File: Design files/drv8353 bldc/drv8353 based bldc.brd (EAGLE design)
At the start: 127 x 127 mm, 115 parts, among them IC1 DRV8353RSRGZT, J3 2X6 FEMALE, J4 B06B-HCMKK

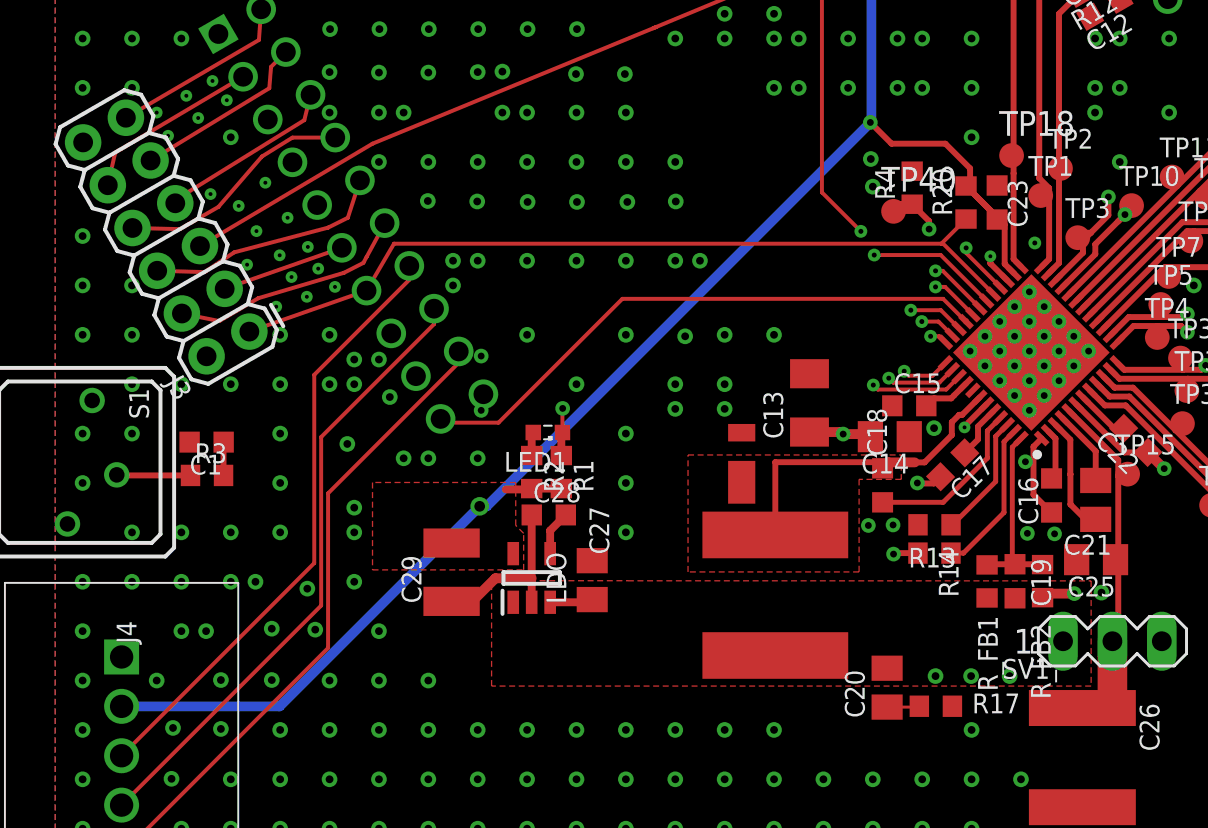
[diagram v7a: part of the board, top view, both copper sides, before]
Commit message: adds zener and bypas header for LDO
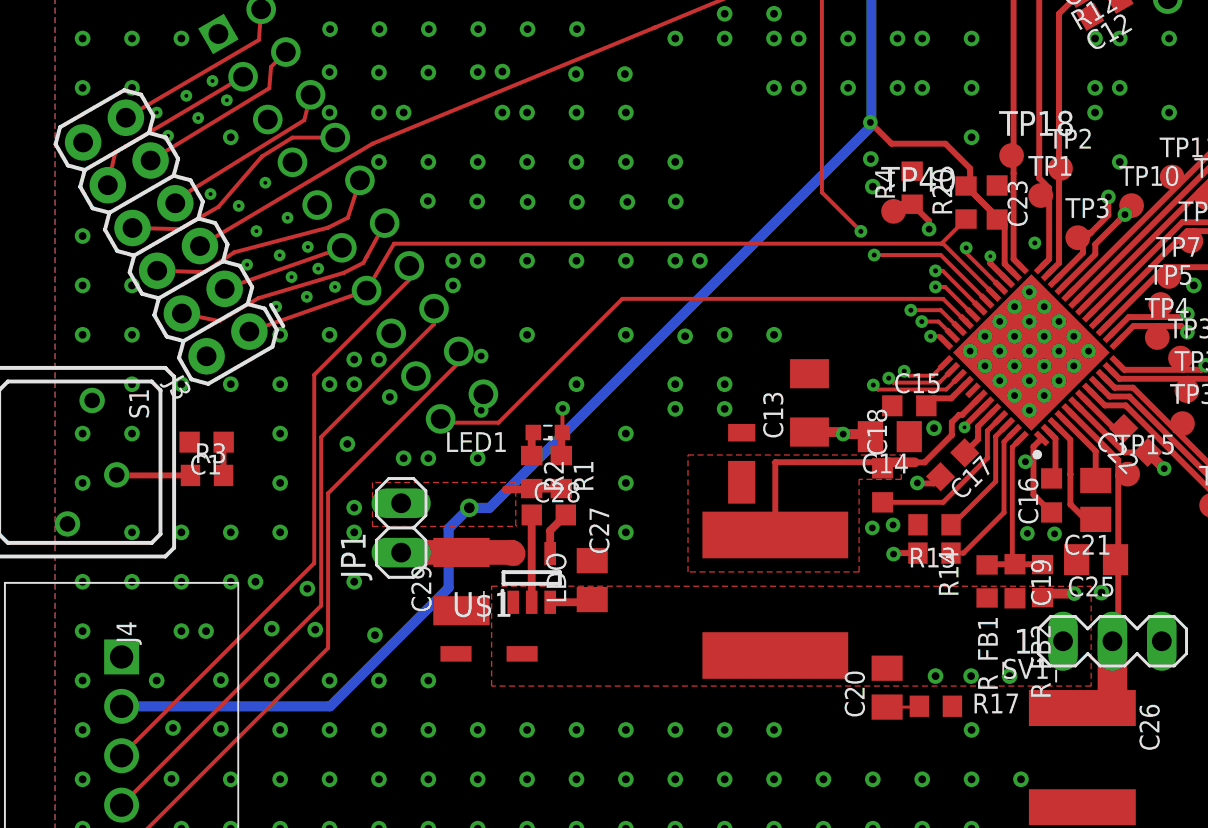
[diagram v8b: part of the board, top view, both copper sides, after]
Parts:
- added JP1: (no value), pinhead:1X02
- added U$1: ZENER, REV BLDC:SOD123
- moved C29 0.70 mm to (24.6, 69.9)
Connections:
- removed net N$5: C28.1, C29.1, LDO.2
- new net N$2: C29.2, JP1.1, LDO.5
- net 3V3: now also JP1.2; no longer C29.2, LDO.5
- net GND: now also C28.1, C29.1, LDO.2, U$1.1
- net VBUCK: now also U$1.2
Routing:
- net N$5: track 9.11 -> 0.00 mm
- net N$2: track 0.00 -> 5.79 mm
- net GND: track 7.95 -> 12.5 mm
- net 3V3: track 101.9 -> 103.8 mm
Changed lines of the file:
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@@
 <attribute name="SPICEPREFIX" value="C" x="72.2346" y="-49.9038" size="1.778" layer="27" display="off"/>
 </element>
-<element name="C29" library="rcl" library_urn="urn:adsk.eagle:library:334" package="C1210K" package3d_urn="urn:adsk.eagle:package:23683/2" value="4.7 uF" x="24.0556" y="70.3408" smashed="yes" rot="R90">
-<attribute name="NAME" x="22.5056" y="68.7408" size="1.016" layer="25" rot="R90"/>
-<attribute name="POPULARITY" value="0" x="124.3856" y="112.2508" size="1.778" layer="27" rot="R90" display="off"/>
-<attribute name="SPICEPREFIX" value="C" x="124.3856" y="112.2508" size="1.778" layer="27" rot="R90" display="off"/>
+<element name="C29" library="rcl" library_urn="urn:adsk.eagle:library:334" package="C1210K" package3d_urn="urn:adsk.eagle:package:23683/2" value="4.7 uF" x="24.5636" y="69.8582" smashed="yes" rot="R90">
+<attribute name="NAME" x="23.0136" y="68.2582" size="1.016" layer="25" rot="R90"/>
+<attribute name="POPULARITY" value="0" x="124.8936" y="111.7682" size="1.778" layer="27" rot="R90" display="off"/>
+<attribute name="SPICEPREFIX" value="C" x="124.8936" y="111.7682" size="1.778" layer="27" rot="R90" display="off"/>
 </element>
 <element name="C30" library="rcl" library_urn="urn:adsk.eagle:library:334" package="C1206" package3d_urn="urn:adsk.eagle:package:23618/2" value="1uF" x="79.2208" y="97.1468" smashed="yes" rot="R180">
@@
 </element>
 <element name="LED1" library="eagle-ltspice" library_urn="urn:adsk.eagle:library:217" package="LED_SML0603" package3d_urn="urn:adsk.eagle:package:13315/1" value="" x="29.0078" y="77.5258" smashed="yes" rot="R180">
-<attribute name="NAME" x="30.0078" y="76.5258" size="1.016" layer="25" rot="R180"/>
+<attribute name="NAME" x="26.9598" y="77.5418" size="1.016" layer="25" rot="R180"/>
 <attribute name="SPICEMODEL" value="NONE" x="-4.0122" y="215.9558" size="1.778" layer="27" rot="R180" display="off"/>
 <attribute name="SPICEPREFIX" value="D" x="-4.0122" y="215.9558" size="1.778" layer="27" rot="R180" display="off"/>
@@
 <attribute name="VALUE" x="91.821" y="111.379" size="1.27" layer="27" rot="R180"/>
 </element>
+<element name="U$1" library="REV BLDC" package="SOD123" package3d_urn="urn:adsk.eagle:package:26308/2" value="ZENER" x="25.9842" y="66.1416" smashed="yes">
+<attribute name="NAME" x="24.0792" y="68.0466" size="1.27" layer="25"/>
+<attribute name="VALUE" x="24.0792" y="62.9666" size="1.27" layer="27"/>
+</element>
+<element name="JP1" library="pinhead" library_urn="urn:adsk.eagle:library:325" package="1X02" package3d_urn="urn:adsk.eagle:package:22435/2" value="" x="21.463" y="72.6186" smashed="yes" rot="R90">
+<attribute name="NAME" x="19.6342" y="70.0024" size="1.27" layer="25" ratio="10" rot="R90"/>
+<attribute name="POPULARITY" value="98" x="21.463" y="72.6186" size="1.778" layer="27" rot="R90" display="off"/>
+<attribute name="VALUE" x="24.638" y="70.0786" size="1.27" layer="27" rot="R90"/>
+</element>
 </elements>
 <signals>
@@
 <vertex x="57.3278" y="12.1158"/>
 </polygon>
-<via x="45.4914" y="72.7456" extent="1-16" drill="0.35"/>
+<via x="45.6946" y="72.6186" extent="1-16" drill="0.35"/>
 <polygon width="0.3048" layer="1" thermals="no">
 <vertex x="3.7338" y="2.9718"/>
@@
 <via x="7.62" y="85.09" extent="1-16" drill="0.4"/>
 <via x="5.08" y="87.63" extent="1-16" drill="0.4"/>
-<via x="20.32" y="67.31" extent="1-16" drill="0.4"/>
+<via x="20.1168" y="67.1068" extent="1-16" drill="0.4"/>
 <via x="33.02" y="72.39" extent="1-16" drill="0.4"/>
 <via x="33.02" y="74.93" extent="1-16" drill="0.4"/>
@@
 <wire x1="54.6602" y1="69.2404" x2="56.0832" y2="69.2404" width="0.508" layer="1"/>
 <via x="48.8696" y="77.7494" extent="1-16" drill="0.4"/>
+<contactref element="U$1" pad="1"/>
+<contactref element="LDO" pad="2"/>
+<contactref element="C28" pad="1"/>
+<contactref element="C29" pad="1"/>
+<wire x1="28.1758" y1="68.7944" x2="28.1758" y2="73.2824" width="0.4064" layer="1"/>
+<wire x1="28.1758" y1="73.2824" x2="28.1796" y2="73.2862" width="0.4064" layer="1"/>
+<wire x1="24.5636" y1="68.3582" x2="24.6398" y2="68.3582" width="0.508" layer="1"/>
 </signal>
 <signal name="SNA">
@@
 <polygon width="0.1524" layer="1" isolate="0.254" thermals="no">
 <vertex x="26.1138" y="64.486"/>
-<vertex x="26.1138" y="69.9034"/>
-<vertex x="33.1216" y="69.9034"/>
-<vertex x="33.1216" y="69.900275"/>
-<vertex x="56.9484" y="69.894834375"/>
+<vertex x="26.1138" y="69.620875"/>
+<vertex x="56.9484" y="69.615428125"/>
+<vertex x="56.9484" y="69.615428125"/>
 <vertex x="56.9484" y="64.486"/>
 </polygon>
 <wire x1="31.2898" y1="68.9334" x2="31.1508" y2="68.7944" width="0.4064" layer="1"/>
 <wire x1="31.1508" y1="68.7944" x2="29.1258" y2="68.7944" width="0.4064" layer="1"/>
+<contactref element="U$1" pad="2"/>
 </signal>
 <signal name="FB">
@@
 <contactref element="R2" pad="2"/>
 <contactref element="U$2" pad="1"/>
-<contactref element="LDO" pad="5"/>
-<contactref element="C29" pad="2"/>
 <contactref element="IC1" pad="26"/>
 <polygon width="0.127" layer="1" thermals="no">
-<vertex x="19.9898" y="70.4596"/>
-<vertex x="27.7622" y="70.4596"/>
-<vertex x="27.7622" y="72.3392"/>
+<vertex x="19.9898" y="72.6948"/>
+<vertex x="27.4066" y="72.6948"/>
 <vertex x="27.3558" y="72.7456"/>
 <vertex x="27.3558" y="74.9554"/>
@@
 </polygon>
 <contactref element="J4" pad="2"/>
-<wire x1="7.0848" y1="63.4418" x2="15.214" y2="63.4418" width="0.508" layer="16"/>
-<wire x1="25.5016" y1="73.7294" x2="15.214" y2="63.4418" width="0.508" layer="16"/>
-<via x="25.5016" y="73.7294" extent="1-16" drill="0.55"/>
-<wire x1="45.6438" y1="93.516" x2="25.8572" y2="73.7294" width="0.508" layer="16"/>
-<wire x1="25.5016" y1="73.7294" x2="25.8572" y2="73.7294" width="0.508" layer="16"/>
+<wire x1="7.0848" y1="63.4418" x2="17.8048" y2="63.4418" width="0.508" layer="16"/>
+<wire x1="24.9682" y1="73.6532" x2="23.9014" y2="72.5864" width="0.508" layer="16"/>
+<wire x1="23.9014" y1="72.5864" x2="23.9014" y2="69.5384" width="0.508" layer="16"/>
+<wire x1="23.9014" y1="69.5384" x2="17.8048" y2="63.4418" width="0.508" layer="16"/>
+<via x="24.9682" y="73.6532" extent="1-16" drill="0.55"/>
+<wire x1="45.6438" y1="93.2874" x2="45.6438" y2="93.516" width="0.508" layer="16"/>
 <wire x1="45.6438" y1="93.516" x2="45.6438" y2="118.5926" width="0.508" layer="16"/>
 <wire x1="48.387" y1="121.3358" x2="45.6438" y2="118.5926" width="0.508" layer="16"/>
@@
 <wire x1="50.5134" y1="90.2042" x2="52.1136" y2="88.604" width="0.3048" layer="1"/>
 <wire x1="52.1136" y1="88.604" x2="52.1136" y2="88.4792" width="0.3048" layer="1"/>
+<contactref element="JP1" pad="2"/>
+<wire x1="24.9682" y1="73.6532" x2="26.0096" y2="73.6532" width="0.508" layer="16"/>
+<wire x1="26.0096" y1="73.6532" x2="45.6438" y2="93.2874" width="0.508" layer="16"/>
 </signal>
 <signal name="ENABLE">
@@
 </polygon>
 </signal>
-<signal name="N$5">
-<contactref element="LDO" pad="2"/>
-<contactref element="C28" pad="1"/>
-<contactref element="C29" pad="1"/>
-<wire x1="28.1758" y1="68.7944" x2="28.1758" y2="70.0278" width="0.4064" layer="1"/>
-<wire x1="28.1758" y1="70.0278" x2="28.1758" y2="73.2824" width="0.4064" layer="1"/>
-<wire x1="28.1758" y1="73.2824" x2="28.1796" y2="73.2862" width="0.4064" layer="1"/>
-<wire x1="24.0556" y1="68.8408" x2="25.1224" y2="68.8408" width="0.508" layer="1"/>
-<wire x1="26.3094" y1="70.0278" x2="25.1224" y2="68.8408" width="0.508" layer="1"/>
-<wire x1="26.3094" y1="70.0278" x2="28.1758" y2="70.0278" width="0.508" layer="1"/>
-</signal>
 <signal name="N$13">
 <contactref element="LDO" pad="4"/>
@@
 <wire x1="56.4896" y1="119.36735" x2="55.917671875" y2="119.939278125" width="0.3048" layer="1"/>
 </signal>
+<signal name="N$2">
+<contactref element="LDO" pad="5"/>
+<contactref element="C29" pad="2"/>
+<contactref element="JP1" pad="1"/>
+<wire x1="27.2258" y1="71.2944" x2="27.162" y2="71.3582" width="1.27" layer="1"/>
+<wire x1="27.162" y1="71.3582" x2="24.5636" y2="71.3582" width="1.27" layer="1"/>
+<wire x1="24.5636" y1="71.3582" x2="21.4726" y2="71.3582" width="1.27" layer="1"/>
+<wire x1="21.4726" y1="71.3582" x2="21.463" y2="71.3486" width="1.27" layer="1"/>
+</signal>
 </signals>
